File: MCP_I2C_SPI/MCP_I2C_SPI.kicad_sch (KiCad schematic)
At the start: 12 parts, among them J10 VCC, J11 GND, J21 V0, J22 Ext, J3 Data, J4 Control, J5 Zlacze_LCD, J6 VSS, J7 K, J8 VDD, J9 A

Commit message: Płytka MCP_I2C_SPIv1 gotowa
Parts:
- added C3, C4: 100n, Library:C_Disc_D8.0mm_W2.5mm_P5.00mm_kwadart, symbol Device:C
- added J26: I2C, Library:PinSocket_1x02_P2.54mm_Vertical_square, symbol Connector:Conn_01x02_Pin
- added J30: Interrupt0, Library:PinSocket_1x03_P2.54mm_Vertical, symbol Connector:Conn_01x03_Pin
- added J34, J45: A2, Library:PinSocket_1x03_P2.54mm_Vertical, symbol Connector:Conn_01x03_Pin
- added J35: SDA, Library:PinSocket_1x03_P2.54mm_Vertical, symbol Connector:Conn_01x03_Pin
- added J36, J46: GPB, Library:PinSocket_1x08_P2.54mm_Vertical_kwadrat, symbol Connector:Conn_01x08_Pin
- added J37, J47: GPA, Library:PinSocket_1x08_P2.54mm_Vertical_kwadrat, symbol Connector:Conn_01x08_Pin
- added J38, J48: A1, Library:PinSocket_1x03_P2.54mm_Vertical, symbol Connector:Conn_01x03_Pin
- added J39: SCK, Library:PinSocket_1x03_P2.54mm_Vertical, symbol Connector:Conn_01x03_Pin
- added J40, J49: A0, Library:PinSocket_1x03_P2.54mm_Vertical, symbol Connector:Conn_01x03_Pin
- added J41, J50: INTA, Library:PinSocket_1x03_P2.54mm_Vertical, symbol Connector:Conn_01x03_Pin
- added J42, J51: INTB, Library:PinSocket_1x03_P2.54mm_Vertical, symbol Connector:Conn_01x03_Pin
- added J43: SPI, Connector_PinSocket_2.54mm:PinSocket_1x04_P2.54mm_Vertical, symbol Connector:Conn_01x04_Pin
- added J44: InterruptS, Library:PinSocket_1x03_P2.54mm_Vertical, symbol Connector:Conn_01x03_Pin
- added R13, R9: 4k7, Library:R_Axial_DIN0207_L6.3mm_D2.5mm_P10.16mm_Horizontal_square, symbol Device:R
- added R14, R15, R16, R17, R18, R19, R20, R8: 10k, Library:R_Axial_DIN0207_L6.3mm_D2.5mm_P10.16mm_Horizontal_square, symbol Device:R
- added U3: MCP23017_SP, Package_DIP:DIP-28_W7.62mm, symbol Interface_Expansion:MCP23017_SP
- added U4: MCP23017_SP, Package_DIP:DIP-28_W7.62mm, symbol Interface_Expansion:MCP23S17_SP
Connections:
- net +5V: now also C3.1, C4.1, R13.1, R14.1, R15.1, R16.1, R17.1, R18.1, R19.1, R20.2, R8.1, R9.1, U3.9 (VDD), U4.9 (VDD)
- net GND: now also C3.2, C4.2, J34.3 (Pin_3), J38.3 (Pin_3), J40.3 (Pin_3), J45.3 (Pin_3), J48.3 (Pin_3), J49.3 (Pin_3), U3.10 (VSS), U4.10 (VSS)
- new net: J45.1 (Pin_1), J48.1 (Pin_1), J49.1 (Pin_1), R20.1
- new net: J42.1 (Pin_1), R15.2
- new net: J41.1 (Pin_1), R14.2
- new net: J51.1 (Pin_1), R19.2
- new net: J35.1 (Pin_1), R13.2
- new net: J39.1 (Pin_1), R9.2
- new net: J34.1 (Pin_1), J38.1 (Pin_1), J40.1 (Pin_1), R16.2
- new net: J48.2 (Pin_2), U4.16 (A1)
- new net: J36.1 (Pin_1), U3.1 (GPB0)
- new net: J36.2 (Pin_2), U3.2 (GPB1)
- new net: J36.3 (Pin_3), U3.3 (GPB2)
- new net: J36.4 (Pin_4), U3.4 (GPB3)
- new net: J36.5 (Pin_5), U3.5 (GPB4)
- new net: J36.6 (Pin_6), U3.6 (GPB5)
- new net: J36.7 (Pin_7), U3.7 (GPB6)
- new net: J36.8 (Pin_8), U3.8 (GPB7)
- new net: J37.1 (Pin_1), U3.21 (GPA0)
- new net: J37.2 (Pin_2), U3.22 (GPA1)
- new net: J37.3 (Pin_3), U3.23 (GPA2)
- new net: J37.4 (Pin_4), U3.24 (GPA3)
- new net: J37.5 (Pin_5), U3.25 (GPA4)
- new net: J37.6 (Pin_6), U3.26 (GPA5)
- new net: J37.7 (Pin_7), U3.27 (GPA6)
- new net: J37.8 (Pin_8), U3.28 (GPA7)
- new net: J45.2 (Pin_2), U4.17 (A2)
- new net: J50.1 (Pin_1), R18.2
- new net: J40.2 (Pin_2), U3.15 (A0)
- new net: J46.1 (Pin_1), U4.1 (GPB0)
- new net: J49.2 (Pin_2), U4.15 (A0)
- new net: J46.2 (Pin_2), U4.2 (GPB1)
- new net: J47.1 (Pin_1), U4.21 (GPA0)
- new net: J47.2 (Pin_2), U4.22 (GPA1)
- new net: J47.3 (Pin_3), U4.23 (GPA2)
- new net: J47.4 (Pin_4), U4.24 (GPA3)
- new net: J47.5 (Pin_5), U4.25 (GPA4)
- new net: J47.6 (Pin_6), U4.26 (GPA5)
- new net: J47.7 (Pin_7), U4.27 (GPA6)
- new net: J47.8 (Pin_8), U4.28 (GPA7)
- new net: J46.3 (Pin_3), U4.3 (GPB2)
- new net: J46.4 (Pin_4), U4.4 (GPB3)
- new net: J46.5 (Pin_5), U4.5 (GPB4)
- new net: J46.6 (Pin_6), U4.6 (GPB5)
- new net: J46.7 (Pin_7), U4.7 (GPB6)
- new net: J46.8 (Pin_8), U4.8 (GPB7)
- new net: J38.2 (Pin_2), U3.16 (A1)
- new net: J34.2 (Pin_2), U3.17 (A2)
- new net CS: J43.1 (Pin_1), U4.11 (~{CS})
- new net INTA0: J30.1 (Pin_1), J41.2 (Pin_2), J41.3 (Pin_3), U3.20 (INTA)
- new net INTAS: J44.1 (Pin_1), J50.2 (Pin_2), J50.3 (Pin_3), U4.20 (INTA)
- new net INTB0: J30.2 (Pin_2), J42.2 (Pin_2), J42.3 (Pin_3), U3.19 (INTB)
- new net INTBS: J44.2 (Pin_2), J51.2 (Pin_2), J51.3 (Pin_3), U4.19 (INTB)
- new net RESET0: J30.3 (Pin_3), R8.2, U3.18 (~{RESET})
- new net RESETS: J44.3 (Pin_3), R17.2, U4.18 (~{RESET})
- new net SCK: J43.2 (Pin_2), U4.12 (SCK)
- new net SCL: J26.2 (Pin_2), J39.2 (Pin_2), J39.3 (Pin_3), U3.12 (SCK)
- new net SDA: J26.1 (Pin_1), J35.2 (Pin_2), J35.3 (Pin_3), U3.13 (SDA)
- new net SI: J43.3 (Pin_3), U4.13 (SI)
- new net SO: J43.4 (Pin_4), U4.14 (SO)
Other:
- removed sheet mcp_i2c
- removed sheet mcp_spi
- moved on the sheet: J10, J11, J21, J22, J3, J4, J5, J6, J7, J8, J9, RV1

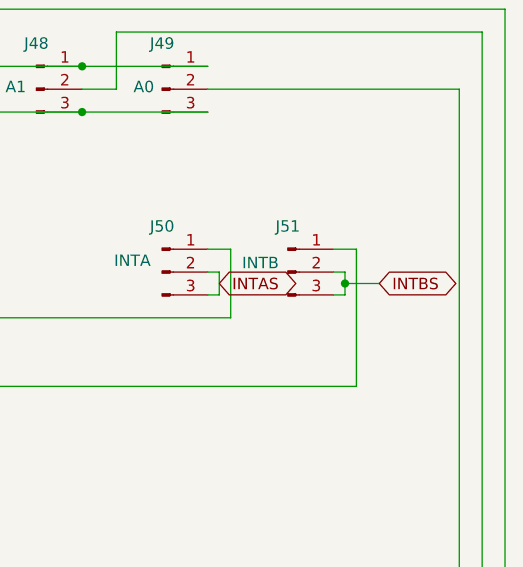
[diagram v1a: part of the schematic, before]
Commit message: Poprawki płytki MCP_I2C_SPI V1
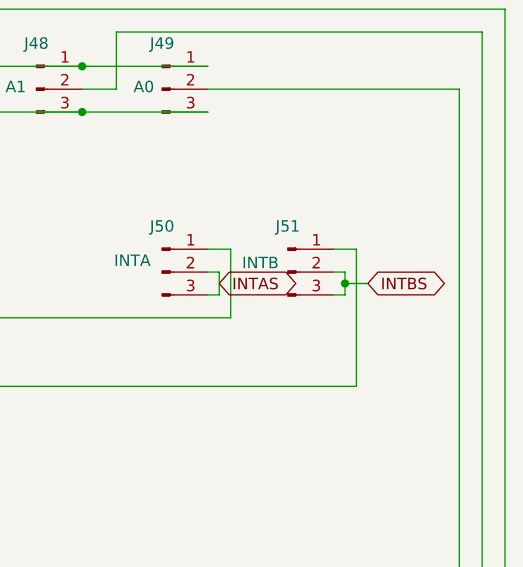
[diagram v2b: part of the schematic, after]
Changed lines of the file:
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@@
 	(wire
 		(pts
-			(xy 265.43 92.71) (xy 269.24 92.71)
+			(xy 265.43 92.71) (xy 267.97 92.71)
 		)
 		(stroke
@@
 	(global_label "INTBS"
 		(shape bidirectional)
-		(at 269.24 92.71 0)
-		(fields_autoplaced yes)
-		(effects
-			(font
-				(size 1.27 1.27)
-			)
-			(justify left)
-		)
-		(property "Intersheetrefs" "${INTERSHEET_REFS}"
-			(at 278.7189 92.71 0)
-			(effects
-				(font
+		(at 267.97 92.71 0)
+		(fields_autoplaced yes)
+		(effects
+			(font
+				(size 1.27 1.27)
+			)
+			(justify left)
+		)
+		(property "Intersheetrefs" "${INTERSHEET_REFS}"
+			(at 277.4489 92.71 0)
+			(effects
+				(font

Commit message: MCP_I2C_SPI_PCB_V6
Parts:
- added J65: SIL6, Connector_PinSocket_2.54mm:PinSocket_1x06_P2.54mm_Vertical, symbol Connector:Conn_01x06_Pin
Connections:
- net +5V: now also J65.1 (Pin_1)
- net RESET0: now also J65.6 (Pin_6)
- net at J42.1 (Pin_1), R15.2: now also J65.5 (Pin_5)
- net at J41.1 (Pin_1), R14.2: now also J65.4 (Pin_4)
- net at J35.1 (Pin_1), R13.2: now also J65.3 (Pin_3)
- net at J39.1 (Pin_1), R9.2: now also J65.2 (Pin_2)

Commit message: Płytka MCP_I2C_SPI_V7
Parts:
- removed J65: SIL6, Connector_PinSocket_2.54mm:PinSocket_1x06_P2.54mm_Vertical, symbol Connector:Conn_01x06_Pin
- added J65: SIL7, Connector_PinSocket_2.54mm:PinSocket_1x07_P2.54mm_Vertical, symbol Connector:Conn_01x07_Pin
- added J66: SIL5, Connector_PinSocket_2.54mm:PinSocket_1x05_P2.54mm_Vertical, symbol Connector:Conn_01x05_Pin
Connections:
- net RESETS is gone; now on net GND: J44.3 (Pin_3), R17.2, U4.18 (~{RESET})
- net +5V: now also J65.1 (Pin_1), J66.1 (Pin_1)
- net GND: now also J66.5 (Pin_5)
- net RESET0: now also J65.6 (Pin_6)
- net at J45.1 (Pin_1), J48.1 (Pin_1), J49.1 (Pin_1)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: now also J66.4 (Pin_4)
- net at J42.1 (Pin_1), R15.2: now also J65.5 (Pin_5)
- net at J41.1 (Pin_1), R14.2: now also J65.4 (Pin_4)
- net at J51.1 (Pin_1), R19.2: now also J66.3 (Pin_3)
- net at J35.1 (Pin_1), R13.2: now also J65.3 (Pin_3)
- net at J39.1 (Pin_1), R9.2: now also J65.2 (Pin_2)
- net at J34.1 (Pin_1), J38.1 (Pin_1), J40.1 (Pin_1)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: now also J65.7 (Pin_7)
- net at J50.1 (Pin_1), R18.2: now also J66.2 (Pin_2)
